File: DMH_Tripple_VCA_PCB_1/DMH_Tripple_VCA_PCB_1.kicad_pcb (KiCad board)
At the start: 2 copper layers, 48 x 175 mm, 0 parts

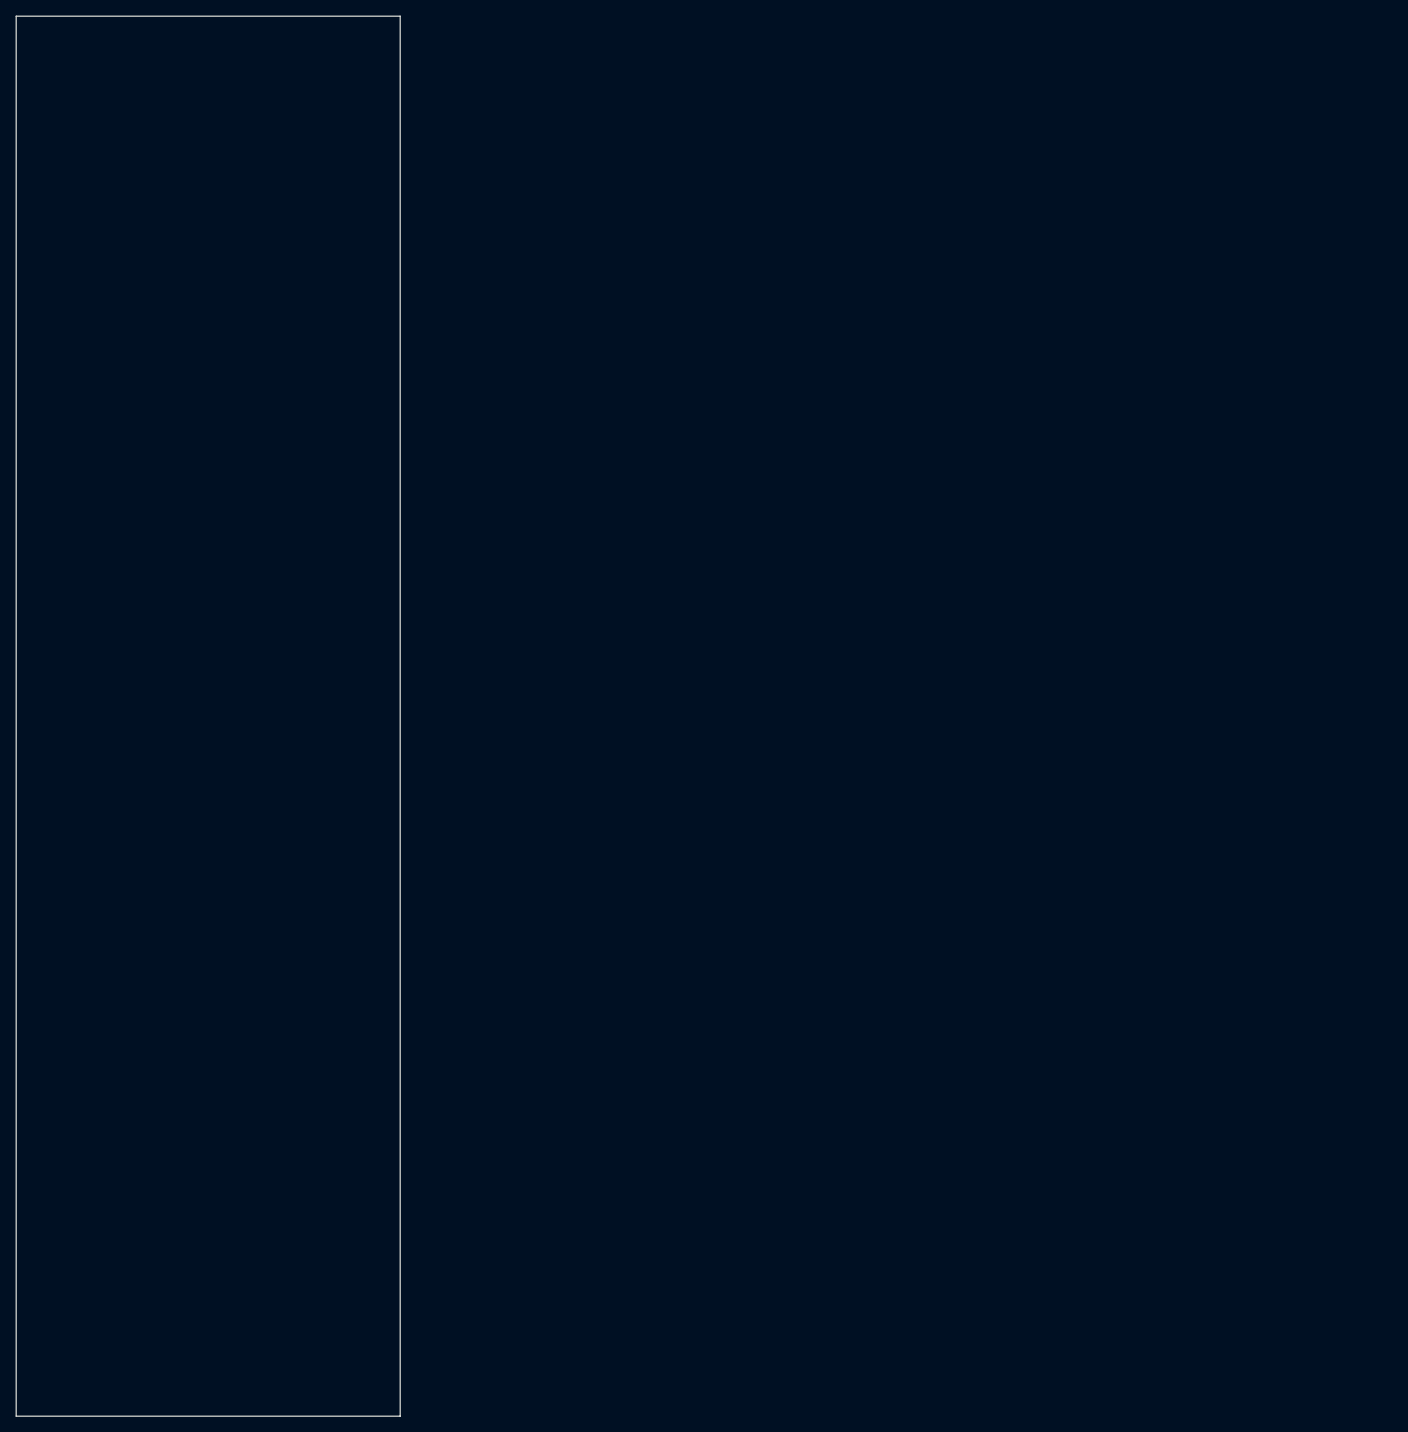
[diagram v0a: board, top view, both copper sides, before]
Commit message: PCB 1 component positioning ongoing
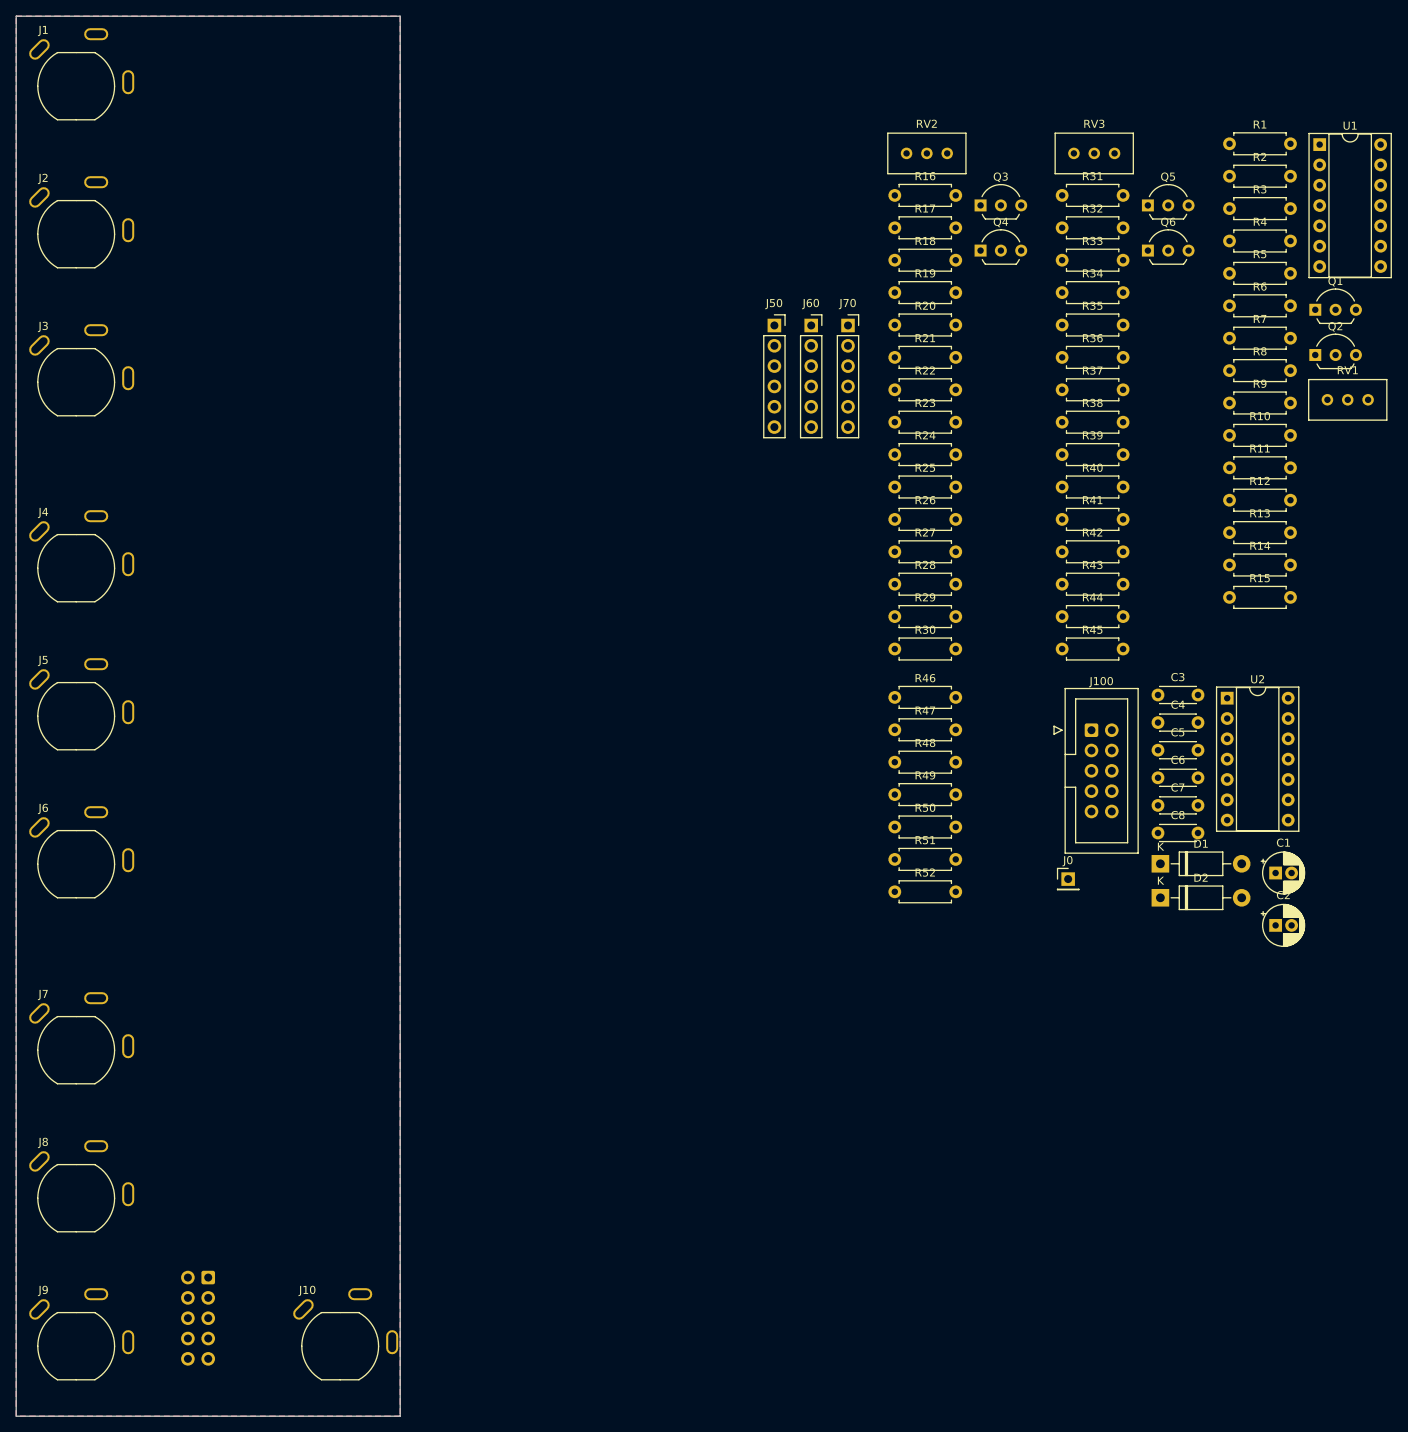
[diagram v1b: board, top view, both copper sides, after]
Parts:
- added C1: 47uF, Capacitor_THT:CP_Radial_D5.0mm_P2.00mm, F.Cu at (208.4, 149.6)
- added C2: 47uF, Capacitor_THT:CP_Radial_D5.0mm_P2.00mm, F.Cu at (208.4, 156.2)
- added C3: 100nF, Capacitor_THT:C_Disc_D4.3mm_W1.9mm_P5.00mm, F.Cu at (193.7, 127.3)
- added C4: 100nF, Capacitor_THT:C_Disc_D4.3mm_W1.9mm_P5.00mm, F.Cu at (193.7, 130.8)
- added C5: 100nF, Capacitor_THT:C_Disc_D4.3mm_W1.9mm_P5.00mm, F.Cu at (193.7, 134.2)
- added C6: 100nF, Capacitor_THT:C_Disc_D4.3mm_W1.9mm_P5.00mm, F.Cu at (193.7, 137.7)
- added C7: 100nF, Capacitor_THT:C_Disc_D4.3mm_W1.9mm_P5.00mm, F.Cu at (193.7, 141.2)
- added C8: 100nF, Capacitor_THT:C_Disc_D4.3mm_W1.9mm_P5.00mm, F.Cu at (193.7, 144.6)
- added D1: SB140+, Diode_THT:D_DO-41_SOD81_P10.16mm_Horizontal, F.Cu at (194.0, 148.4)
- added D2: SB140-, Diode_THT:D_DO-41_SOD81_P10.16mm_Horizontal, F.Cu at (194.0, 152.7)
- added J0: Conn_01x01, Connector_PinHeader_2.54mm:PinHeader_1x01_P2.54mm_Vertical, F.Cu at (182.5, 150.4)
- added J1: TS_Jack_6.35mm_Sw, SynthStuff:CUI_MJ-63052A, F.Cu at (58.5, 51.2)
- added J10: TS_Jack_6.35mm_Sw, SynthStuff:CUI_MJ-63052A, F.Cu at (91.5, 208.8)
- added J100: IDC_02x05, SynthStuff:IDC-Header_2x05_P2.54mm_Vertical_Eurorack, F.Cu at (185.4, 131.8)
- added J2: TS_Jack_6.35mm_Sw, SynthStuff:CUI_MJ-63052A, F.Cu at (58.5, 69.8)
- added J200: IDC_02x05, SynthStuff:IDC-Header_2x05_P2.54mm_Vertical_BackBone, B.Cu at (75.0, 200.2)
- added J3: TS_Jack_6.35mm_Sw, SynthStuff:CUI_MJ-63052A, F.Cu at (58.5, 88.2)
- added J4: TS_Jack_6.35mm_Sw, SynthStuff:CUI_MJ-63052A, F.Cu at (58.5, 111.5)
- added J5: TS_Jack_6.35mm_Sw, SynthStuff:CUI_MJ-63052A, F.Cu at (58.5, 130.0)
- added J50: Conn_01x06, Connector_PinSocket_2.54mm:PinSocket_1x06_P2.54mm_Vertical, F.Cu at (145.8, 81.2)
- added J6: TS_Jack_6.35mm_Sw, SynthStuff:CUI_MJ-63052A, F.Cu at (58.5, 148.5)
- added J60: Conn_01x06, Connector_PinSocket_2.54mm:PinSocket_1x06_P2.54mm_Vertical, F.Cu at (150.4, 81.2)
- added J7: TS_Jack_6.35mm_Sw, SynthStuff:CUI_MJ-63052A, F.Cu at (58.5, 171.8)
- added J70: Conn_01x06, Connector_PinSocket_2.54mm:PinSocket_1x06_P2.54mm_Vertical, F.Cu at (155.0, 81.2)
- added J8: TS_Jack_6.35mm_Sw, SynthStuff:CUI_MJ-63052A, F.Cu at (58.5, 190.2)
- added J9: TS_Jack_6.35mm_Sw, SynthStuff:CUI_MJ-63052A, F.Cu at (58.5, 208.8)
- added Q1: BC548, Package_TO_SOT_THT:TO-92L_Inline_Wide, F.Cu at (213.4, 79.2)
- added Q2: BC548, Package_TO_SOT_THT:TO-92L_Inline_Wide, F.Cu at (213.4, 84.8)
- added Q3: BC548, Package_TO_SOT_THT:TO-92L_Inline_Wide, F.Cu at (171.5, 66.2)
- added Q4: BC548, Package_TO_SOT_THT:TO-92L_Inline_Wide, F.Cu at (171.5, 71.8)
- added Q5: BC548, Package_TO_SOT_THT:TO-92L_Inline_Wide, F.Cu at (192.5, 66.2)
- added Q6: BC548, Package_TO_SOT_THT:TO-92L_Inline_Wide, F.Cu at (192.5, 71.8)
- added R1: 20k, Resistor_THT:R_Axial_DIN0207_L6.3mm_D2.5mm_P7.62mm_Horizontal, F.Cu at (202.7, 58.5)
- added R10: 100R, Resistor_THT:R_Axial_DIN0207_L6.3mm_D2.5mm_P7.62mm_Horizontal, F.Cu at (202.7, 94.9)
- added R11: 100R, Resistor_THT:R_Axial_DIN0207_L6.3mm_D2.5mm_P7.62mm_Horizontal, F.Cu at (202.7, 99.0)
- added R12: 10k, Resistor_THT:R_Axial_DIN0207_L6.3mm_D2.5mm_P7.62mm_Horizontal, F.Cu at (202.7, 103.0)
- added R13: 100k, Resistor_THT:R_Axial_DIN0207_L6.3mm_D2.5mm_P7.62mm_Horizontal, F.Cu at (202.7, 107.0)
- added R14: 82k, Resistor_THT:R_Axial_DIN0207_L6.3mm_D2.5mm_P7.62mm_Horizontal, F.Cu at (202.7, 111.1)
- added R15: 100k, Resistor_THT:R_Axial_DIN0207_L6.3mm_D2.5mm_P7.62mm_Horizontal, F.Cu at (202.7, 115.2)
- added R16: 20k, Resistor_THT:R_Axial_DIN0207_L6.3mm_D2.5mm_P7.62mm_Horizontal, F.Cu at (160.8, 64.9)
- added R17: 20k, Resistor_THT:R_Axial_DIN0207_L6.3mm_D2.5mm_P7.62mm_Horizontal, F.Cu at (160.8, 69.0)
- added R18: 100k, Resistor_THT:R_Axial_DIN0207_L6.3mm_D2.5mm_P7.62mm_Horizontal, F.Cu at (160.8, 73.0)
- added R19: 10k, Resistor_THT:R_Axial_DIN0207_L6.3mm_D2.5mm_P7.62mm_Horizontal, F.Cu at (160.8, 77.0)
- added R2: 20k, Resistor_THT:R_Axial_DIN0207_L6.3mm_D2.5mm_P7.62mm_Horizontal, F.Cu at (202.7, 62.5)
- added R20: 1k, Resistor_THT:R_Axial_DIN0207_L6.3mm_D2.5mm_P7.62mm_Horizontal, F.Cu at (160.8, 81.1)
- added R21: 10k, Resistor_THT:R_Axial_DIN0207_L6.3mm_D2.5mm_P7.62mm_Horizontal, F.Cu at (160.8, 85.2)
- added R22: 100k, Resistor_THT:R_Axial_DIN0207_L6.3mm_D2.5mm_P7.62mm_Horizontal, F.Cu at (160.8, 89.2)
- added R23: 100k, Resistor_THT:R_Axial_DIN0207_L6.3mm_D2.5mm_P7.62mm_Horizontal, F.Cu at (160.8, 93.2)
- added R24: 100k, Resistor_THT:R_Axial_DIN0207_L6.3mm_D2.5mm_P7.62mm_Horizontal, F.Cu at (160.8, 97.3)
- added R25: 100R, Resistor_THT:R_Axial_DIN0207_L6.3mm_D2.5mm_P7.62mm_Horizontal, F.Cu at (160.8, 101.3)
- added R26: 100R, Resistor_THT:R_Axial_DIN0207_L6.3mm_D2.5mm_P7.62mm_Horizontal, F.Cu at (160.8, 105.4)
- added R27: 10k, Resistor_THT:R_Axial_DIN0207_L6.3mm_D2.5mm_P7.62mm_Horizontal, F.Cu at (160.8, 109.5)
- added R28: 100k, Resistor_THT:R_Axial_DIN0207_L6.3mm_D2.5mm_P7.62mm_Horizontal, F.Cu at (160.8, 113.5)
- added R29: 82k, Resistor_THT:R_Axial_DIN0207_L6.3mm_D2.5mm_P7.62mm_Horizontal, F.Cu at (160.8, 117.5)
- added R3: 100k, Resistor_THT:R_Axial_DIN0207_L6.3mm_D2.5mm_P7.62mm_Horizontal, F.Cu at (202.7, 66.5)
- added R30: 100k, Resistor_THT:R_Axial_DIN0207_L6.3mm_D2.5mm_P7.62mm_Horizontal, F.Cu at (160.8, 121.6)
- added R31: 20k, Resistor_THT:R_Axial_DIN0207_L6.3mm_D2.5mm_P7.62mm_Horizontal, F.Cu at (181.7, 64.9)
- added R32: 20k, Resistor_THT:R_Axial_DIN0207_L6.3mm_D2.5mm_P7.62mm_Horizontal, F.Cu at (181.7, 69.0)
- added R33: 100k, Resistor_THT:R_Axial_DIN0207_L6.3mm_D2.5mm_P7.62mm_Horizontal, F.Cu at (181.7, 73.0)
- added R34: 10k, Resistor_THT:R_Axial_DIN0207_L6.3mm_D2.5mm_P7.62mm_Horizontal, F.Cu at (181.7, 77.0)
- added R35: 1k, Resistor_THT:R_Axial_DIN0207_L6.3mm_D2.5mm_P7.62mm_Horizontal, F.Cu at (181.7, 81.1)
- added R36: 10k, Resistor_THT:R_Axial_DIN0207_L6.3mm_D2.5mm_P7.62mm_Horizontal, F.Cu at (181.7, 85.2)
- added R37: 100k, Resistor_THT:R_Axial_DIN0207_L6.3mm_D2.5mm_P7.62mm_Horizontal, F.Cu at (181.7, 89.2)
- added R38: 100k, Resistor_THT:R_Axial_DIN0207_L6.3mm_D2.5mm_P7.62mm_Horizontal, F.Cu at (181.7, 93.2)
- added R39: 100k, Resistor_THT:R_Axial_DIN0207_L6.3mm_D2.5mm_P7.62mm_Horizontal, F.Cu at (181.7, 97.3)
- added R4: 10k, Resistor_THT:R_Axial_DIN0207_L6.3mm_D2.5mm_P7.62mm_Horizontal, F.Cu at (202.7, 70.6)
- added R40: 100R, Resistor_THT:R_Axial_DIN0207_L6.3mm_D2.5mm_P7.62mm_Horizontal, F.Cu at (181.7, 101.3)
- added R41: 100R, Resistor_THT:R_Axial_DIN0207_L6.3mm_D2.5mm_P7.62mm_Horizontal, F.Cu at (181.7, 105.4)
- added R42: 10k, Resistor_THT:R_Axial_DIN0207_L6.3mm_D2.5mm_P7.62mm_Horizontal, F.Cu at (181.7, 109.5)
- added R43: 100k, Resistor_THT:R_Axial_DIN0207_L6.3mm_D2.5mm_P7.62mm_Horizontal, F.Cu at (181.7, 113.5)
- added R44: 82k, Resistor_THT:R_Axial_DIN0207_L6.3mm_D2.5mm_P7.62mm_Horizontal, F.Cu at (181.7, 117.5)
- added R45: 100k, Resistor_THT:R_Axial_DIN0207_L6.3mm_D2.5mm_P7.62mm_Horizontal, F.Cu at (181.7, 121.6)
- added R46: 100k, Resistor_THT:R_Axial_DIN0207_L6.3mm_D2.5mm_P7.62mm_Horizontal, F.Cu at (160.8, 127.7)
- added R47: 100k, Resistor_THT:R_Axial_DIN0207_L6.3mm_D2.5mm_P7.62mm_Horizontal, F.Cu at (160.8, 131.7)
- added R48: 100k, Resistor_THT:R_Axial_DIN0207_L6.3mm_D2.5mm_P7.62mm_Horizontal, F.Cu at (160.8, 135.8)
- added R49: 100k, Resistor_THT:R_Axial_DIN0207_L6.3mm_D2.5mm_P7.62mm_Horizontal, F.Cu at (160.8, 139.8)
- added R5: 1k, Resistor_THT:R_Axial_DIN0207_L6.3mm_D2.5mm_P7.62mm_Horizontal, F.Cu at (202.7, 74.7)
- added R50: 100k, Resistor_THT:R_Axial_DIN0207_L6.3mm_D2.5mm_P7.62mm_Horizontal, F.Cu at (160.8, 143.8)
- added R51: 100k, Resistor_THT:R_Axial_DIN0207_L6.3mm_D2.5mm_P7.62mm_Horizontal, F.Cu at (160.8, 147.9)
- added R52: 1k, Resistor_THT:R_Axial_DIN0207_L6.3mm_D2.5mm_P7.62mm_Horizontal, F.Cu at (160.8, 151.9)
- added R6: 10k, Resistor_THT:R_Axial_DIN0207_L6.3mm_D2.5mm_P7.62mm_Horizontal, F.Cu at (202.7, 78.7)
- added R7: 100k, Resistor_THT:R_Axial_DIN0207_L6.3mm_D2.5mm_P7.62mm_Horizontal, F.Cu at (202.7, 82.8)
- added R8: 100k, Resistor_THT:R_Axial_DIN0207_L6.3mm_D2.5mm_P7.62mm_Horizontal, F.Cu at (202.7, 86.8)
- added R9: 100k, Resistor_THT:R_Axial_DIN0207_L6.3mm_D2.5mm_P7.62mm_Horizontal, F.Cu at (202.7, 90.8)
- added RV1: 100k, Potentiometer_THT:Potentiometer_Bourns_3296W_Vertical, F.Cu at (220.0, 90.5)
- added RV2: 100k, Potentiometer_THT:Potentiometer_Bourns_3296W_Vertical, F.Cu at (167.4, 59.6)
- added RV3: 100k, Potentiometer_THT:Potentiometer_Bourns_3296W_Vertical, F.Cu at (188.3, 59.6)
- added U1: TL074, Package_DIP:DIP-14_W7.62mm_Socket, F.Cu at (213.9, 58.5)
- added U2: TL074, Package_DIP:DIP-14_W7.62mm_Socket, F.Cu at (202.4, 127.8)
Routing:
- added copper zone on B.Cu, net GND
- added copper zone on F.Cu, net GND

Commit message: PCB 1 component positioning in progress
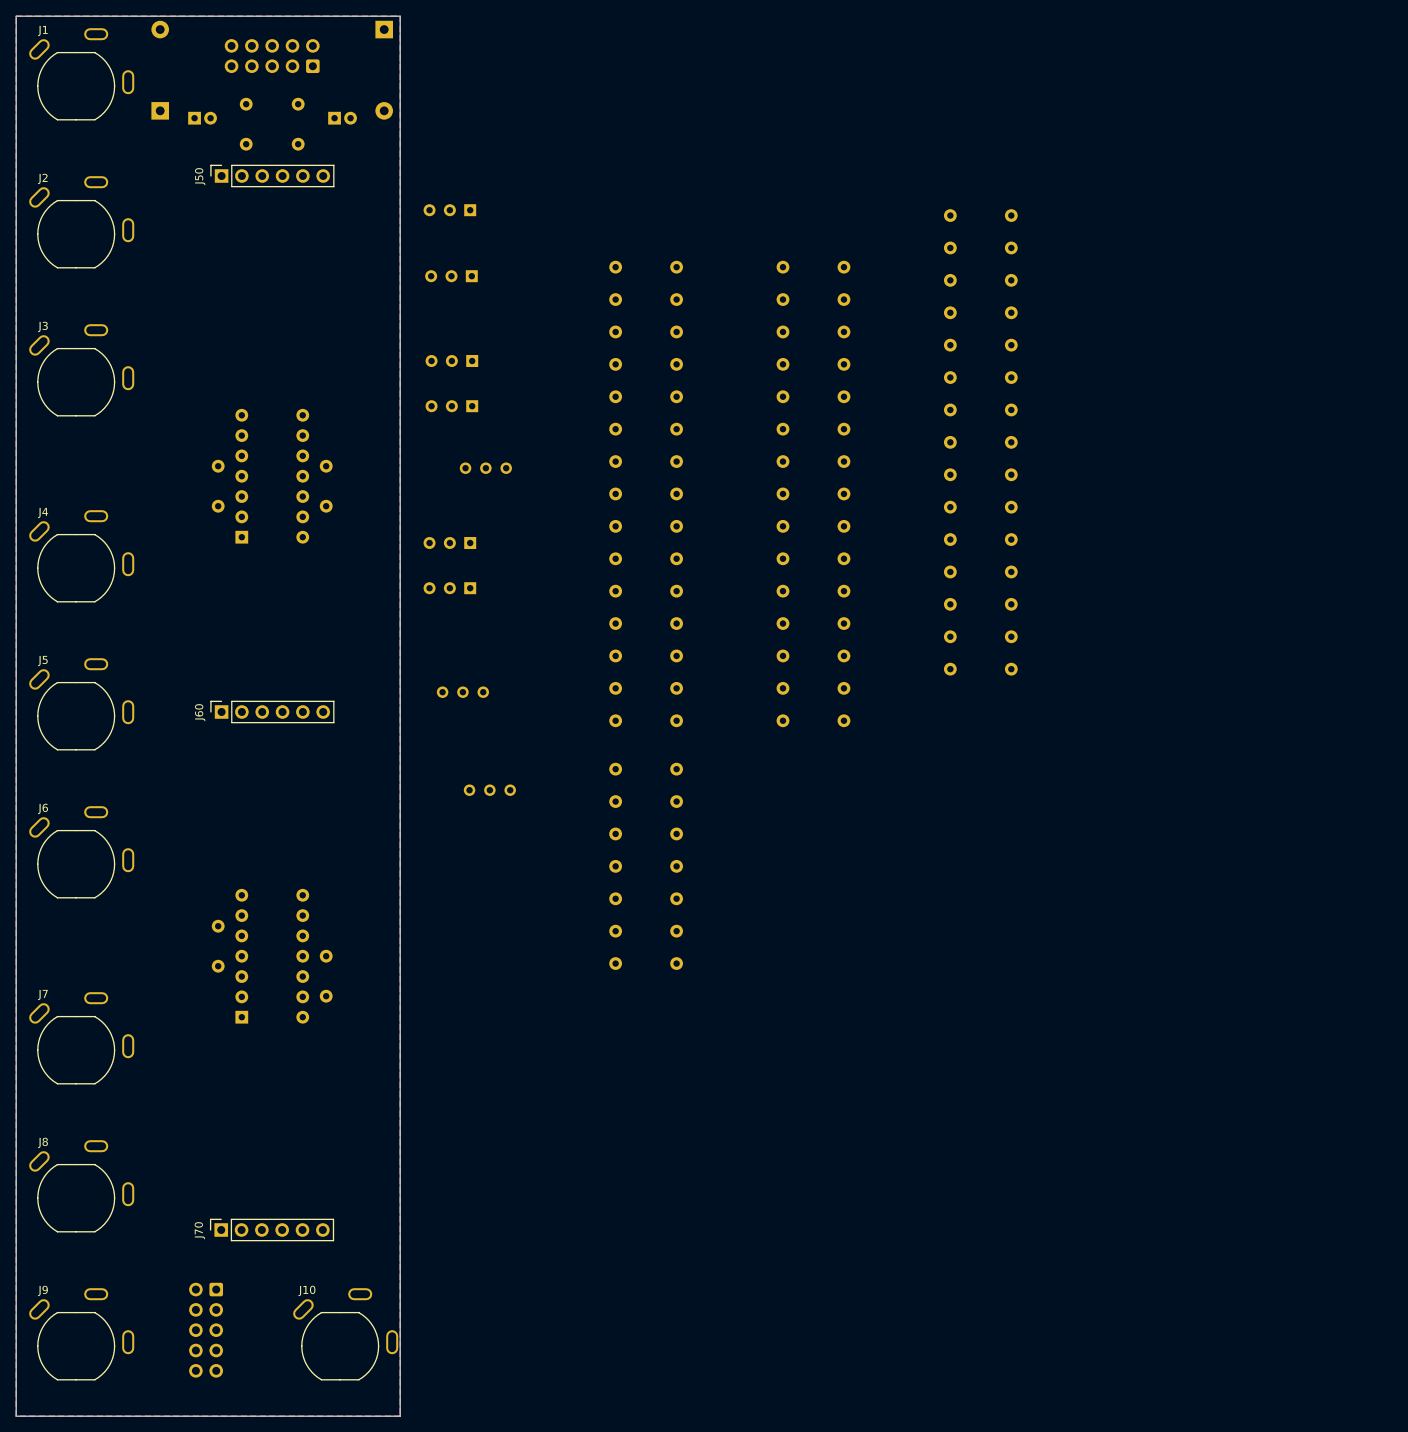
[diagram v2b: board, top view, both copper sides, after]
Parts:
- removed J0: Conn_01x01, Connector_PinHeader_2.54mm:PinHeader_1x01_P2.54mm_Vertical
- C1, C2, C3, C4, C5, C6, C7, C8, D1, D2, J100, Q1, Q2, Q3, Q4, Q5, Q6, R1, R10, R11, R12, R13, R14, R15, R16, R17, R18, R19, R2, R20, R21, R22, R23, R24, R25, R26, R27, R28, R29, R3, R30, R31, R32, R33, R34, R35, R36, R37, R38, R39, R4, R40, R41, R42, R43, R44, R45, R46, R47, R48, R49, R5, R50, R51, R52, R6, R7, R8, R9, RV1, RV2, RV3, U1, U2: moved to B.Cu
- moved C1 164.8 mm to (73.3, 55.2)
- moved D1 156.5 mm to (69.0, 54.3), turned to 90 degrees
- moved C2 155.0 mm to (90.8, 55.2)
- moved D2 145.6 mm to (97.0, 44.2), turned to -90 degrees
- moved U1 143.4 mm to (79.2, 107.6)
- moved J70 137.6 mm to (76.6, 194.2), turned to 90 degrees
- moved C3 133.2 mm to (79.8, 58.5), turned to 90 degrees
- moved C4 132.4 mm to (86.2, 53.5), turned to -90 degrees
- moved U2 129.5 mm to (79.2, 167.6)
- moved J100 127.9 mm to (88.1, 48.8), turned to 90 degrees
- moved C5 122.7 mm to (76.2, 98.8), turned to -90 degrees
- moved C7 119.2 mm to (76.2, 161.2), turned to 90 degrees
- moved RV3 113.3 mm to (107.7, 139.2), turned to 180 degrees
- moved RV1 113.1 mm to (107.2, 99.0), turned to 180 degrees
- moved Q2 109.6 mm to (107.8, 114.0), turned to 180 degrees
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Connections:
- R13 pad 2: Net-(U1A--) -> Net-(U1B--)
- R14 pad 1: Net-(U1A--) -> Net-(U1B--)
- R15 pad 2: Net-(U1A--) -> Net-(U1B--)
- R18 pad 2: Net-(U1C--) -> Net-(U1D--)
- R19 pad 1: Net-(U1C--) -> Net-(U1D--)
- R21 pad 1: Net-(U1C-+) -> Net-(U1D-+)
- R22 pad 1: Net-(U1C-+) -> Net-(U1D-+)
- R28 pad 2: Net-(U1B--) -> Net-(U1A--)
- R29 pad 1: Net-(U1B--) -> Net-(U1A--)
- R3 pad 2: Net-(U1D--) -> Net-(U1C--)
- R30 pad 2: Net-(U1B--) -> Net-(U1A--)
- R33 pad 2: Net-(U2D--) -> Net-(U2C--)
- R34 pad 1: Net-(U2D--) -> Net-(U2C--)
- R36 pad 1: Net-(U2D-+) -> Net-(U2C-+)
- R37 pad 1: Net-(U2D-+) -> Net-(U2C-+)
- R4 pad 1: Net-(U1D--) -> Net-(U1C--)
- R43 pad 2: Net-(U2A--) -> Net-(U2B--)
- R44 pad 1: Net-(U2A--) -> Net-(U2B--)
- R45 pad 2: Net-(U2A--) -> Net-(U2B--)
- R46 pad 2: Net-(U2B-+) -> Net-(U2A-+)
- R47 pad 1: Net-(U2B-+) -> Net-(U2A-+)
- R48 pad 2: Net-(U2B-+) -> Net-(U2A-+)
- R49 pad 2: Net-(U2B-+) -> Net-(U2A-+)
- R50 pad 2: Net-(U2C-+) -> Net-(U2D-+)
- R51 pad 1: Net-(U2C-+) -> Net-(U2D-+)
- R6 pad 1: Net-(U1D-+) -> Net-(U1C-+)
- R7 pad 1: Net-(U1D-+) -> Net-(U1C-+)
- U1 pad 1: Net-(R12-Pad1) -> Net-(R27-Pad1)
- U1 pad 14: Net-(R3-Pad1) -> Net-(R18-Pad1)
- U1 pad 7: Net-(R27-Pad1) -> Net-(R12-Pad1)
- U1 pad 8: Net-(R18-Pad1) -> Net-(R3-Pad1)
- U2 pad 1: Net-(R42-Pad1) -> Net-(R47-Pad2)
- U2 pad 13: Net-(U2D--) -> GND
- U2 pad 14: Net-(R33-Pad1) -> Net-(R51-Pad2)
- U2 pad 2: Net-(U2A--) -> GND
- U2 pad 3: GND -> Net-(U2A-+)
- U2 pad 5: Net-(U2B-+) -> GND
- U2 pad 6: GND -> Net-(U2B--)
- U2 pad 7: Net-(R47-Pad2) -> Net-(R42-Pad1)
- U2 pad 8: Net-(R51-Pad2) -> Net-(R33-Pad1)
- U2 pad 9: GND -> Net-(U2C--)
